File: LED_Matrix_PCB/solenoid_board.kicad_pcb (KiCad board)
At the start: 2 copper layers, 100 x 93 mm, 102 parts, among them J2 MCU_LEFT_LEGS, J3 MCU_RIGHT_LEGS

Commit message: Laid footprint geometry. Need to add a capacitor on the RS-485 Transciever.
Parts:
- moved LED8_0 289.5 mm to (61.4, 156.1)
- moved LED7_2 252.5 mm to (85.4, 145.1)
- moved LED7_1 251.2 mm to (73.4, 145.1)
- moved LED7_0 250.2 mm to (61.4, 145.1)
- moved LED7_4 242.4 mm to (109.4, 145.1)
- moved LED4_1 238.8 mm to (73.4, 112.1)
- moved LED5_0 236.4 mm to (61.4, 123.1)
- moved LED6_2 235.5 mm to (85.4, 134.1)
- moved LED6_3 231.2 mm to (97.4, 134.1)
- moved LED8_5 229.1 mm to (121.4, 156.1)
- moved LED8_4 227.5 mm to (109.4, 156.1)
- moved LED8_3 226.3 mm to (97.4, 156.1)
- moved LED6_1 225.5 mm to (73.4, 134.1)
- moved LED8_2 225.5 mm to (85.4, 156.1)
- moved LED3_0 225.4 mm to (61.4, 101.1)
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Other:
- board outline removed

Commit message: Routed 90% of wires, still need to re-order the column pin masking to better complement the routing.
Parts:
- removed LED8_0, LED8_1, LED8_2, LED8_3, LED8_4, LED8_5, LED8_6, LED8_7, LED8_8: Screw-terminal, TerminalBlock:TerminalBlock_bornier-2_P5.08mm
- moved GND1 8.07 mm to (219.8, 140.3)
- moved LED0_6 4.93 mm to (138.3, 67.9)
- moved LED0_7 4.93 mm to (150.3, 67.9)
- moved LED0_8 4.93 mm to (162.3, 67.9)
- moved LED1_6 4.93 mm to (138.3, 78.9)
- moved LED1_7 4.93 mm to (150.3, 78.9)
- moved LED1_8 4.93 mm to (162.3, 78.9)
- moved LED2_6 4.93 mm to (138.3, 89.9)
- moved LED2_7 4.93 mm to (150.3, 89.9)
- moved LED2_8 4.93 mm to (162.3, 89.9)
- moved LED3_6 4.93 mm to (138.3, 100.9)
- moved LED3_7 4.93 mm to (150.3, 100.9)
- moved LED3_8 4.93 mm to (162.3, 100.9)
- moved LED4_6 4.93 mm to (138.3, 111.9)
- moved LED4_7 4.93 mm to (150.3, 111.9)
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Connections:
- RS-485 pad 2: /A4 -> /MISO
- RS-485 pad 3: /A4 -> /MISO
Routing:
- net /A0: track 0.00 -> 179.2 mm
- net /MOSI: track 0.00 -> 171.2 mm
- net /A1: track 0.00 -> 168.7 mm
- net /ROW6: track 0.00 -> 165.6 mm
- net /A2: track 0.00 -> 163.1 mm
- net /A4: track 0.00 -> 160.5 mm
- net /A5: track 0.00 -> 160.3 mm
- net /A3: track 0.00 -> 159.7 mm
- net /COL8: track 0.00 -> 85.7 mm
- net /COL6: track 0.00 -> 85.7 mm
- net /COL5: track 0.00 -> 85.7 mm
- net /COL4: track 0.00 -> 85.7 mm
- net /COL1: track 0.00 -> 85.7 mm
- net /COL0: track 0.00 -> 85.7 mm
- net /COL7: track 0.00 -> 85.7 mm
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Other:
- board text added: "Author: Patrick Taliaferro"
- board text removed: "Authors: Patrick Taliaferro"
- board text removed: "Will Tekulve"

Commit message: Placed finishing touches on V1.0
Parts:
- added REF**: MountingHole_2.7mm_M2.5, MountingHole:MountingHole_2.7mm_M2.5, F.Cu at (225.0, 145.0)
- added REF**: MountingHole_2.7mm_M2.5, MountingHole:MountingHole_2.7mm_M2.5, F.Cu at (225.0, 35.0)
- added REF**: MountingHole_2.7mm_M2.5, MountingHole:MountingHole_2.7mm_M2.5, F.Cu at (55.0, 35.0)
- added REF**: MountingHole_2.7mm_M2.5, MountingHole:MountingHole_2.7mm_M2.5, F.Cu at (55.0, 145.0)
- moved +5V_IN1 19.4 mm to (218.5, 47.8)
- moved LED6_6 10.8 mm to (133.5, 124.3)
- moved LED6_7 10.8 mm to (145.5, 124.3)
- moved LED6_8 10.8 mm to (157.5, 124.3)
- moved LED7_6 10.8 mm to (133.5, 135.3)
- moved LED7_7 10.8 mm to (145.5, 135.3)
- moved LED7_8 10.8 mm to (157.5, 135.3)
- moved LED6_0 10.8 mm to (61.5, 124.3)
- moved LED7_0 10.8 mm to (61.5, 135.3)
- moved GND1 10.8 mm to (215.0, 130.6)
- moved J2 10.8 mm to (189.2, 77.9)
- moved LED0_6 10.8 mm to (133.5, 58.3)
- moved LED0_7 10.8 mm to (145.5, 58.3)
- moved LED0_8 10.8 mm to (157.5, 58.3)
- moved LED1_6 10.8 mm to (133.5, 69.3)
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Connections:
- R330 pad 2: /SDA -> /D13
- R331 pad 2: /SCL -> /D12
- R332 pad 2: /D5 -> /D11
- R333 pad 2: /D6 -> /D10
- R335 pad 2: /D10 -> /D6
- R336 pad 2: /D11 -> /D5
- R337 pad 2: /D12 -> /SCL
- R338 pad 2: /D13 -> /SDA
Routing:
- net /D12: track 0.00 -> 209.3 mm, vias 0 -> 2
- net /D13: track 0.00 -> 208.6 mm, vias 0 -> 2
- net /D11: track 0.00 -> 208.6 mm, vias 0 -> 2
- net /D10: track 0.00 -> 164.5 mm
- net /D9: track 0.00 -> 150.8 mm
- net /D6: track 0.00 -> 137.5 mm
- net /D5: track 0.00 -> 124.1 mm
- net /SCL: track 0.00 -> 109.9 mm
- net /SDA: track 0.00 -> 96.3 mm
- net +5V: track 0.00 -> 47.5 mm
- net GND: track 0.00 -> 7.13 mm, vias 0 -> 1
- added copper zone on B.Cu, net GND
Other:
- board outline added: 180 x 120 mm

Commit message: Changed footprints for resistors, changed resistor suppliers, and re-routed wires. Need to add mounting holes and clean for ordering.
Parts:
- removed REF** (x4): MountingHole_2.7mm_M2.5, MountingHole:MountingHole_2.7mm_M2.5
- R10, R11, R330, R331, R332, R333, R334, R335, R336, R337, R338: footprint Resistor_SMD:R_2010_5025Metric_Pad1.52x2.65mm_HandSolder -> Resistor_THT:R_Axial_DIN0309_L9.0mm_D3.2mm_P20.32mm_Horizontal
- moved R10 20.5 mm to (179.3, 143.7)
- moved R11 20.4 mm to (173.7, 141.7)
- moved RJ0 13.8 mm to (191.0, 137.0)
- moved RJ1 13.8 mm to (212.2, 137.0)
- moved R330 13.3 mm to (61.5, 34.0), turned to 0 degrees
- moved R331 9.28 mm to (73.5, 38.0), turned to 0 degrees
- moved R335 9.28 mm to (121.5, 38.0), turned to 0 degrees
- moved R332 5.28 mm to (85.5, 42.0), turned to 0 degrees
- moved R336 5.28 mm to (133.5, 42.0), turned to 0 degrees
- moved R334 2.72 mm to (109.5, 50.0), turned to 0 degrees
- moved R338 2.72 mm to (157.5, 50.0), turned to 0 degrees
- moved GND1 2.15 mm to (215.6, 128.5)
- moved R333 1.28 mm to (97.5, 46.0), turned to 0 degrees
- moved R337 1.28 mm to (145.5, 46.0), turned to 0 degrees
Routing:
- net /D11: track 208.6 -> 156.4 mm, vias 2 -> 0
- net /D12: track 209.3 -> 162.2 mm, vias 2 -> 0
- net /D13: track 208.6 -> 172.9 mm, vias 2 -> 0
- net /D10: track 164.5 -> 144.7 mm
- net /D9: track 150.8 -> 131.6 mm
- net /D6: track 137.5 -> 119.4 mm
- net /D5: track 124.1 -> 106.7 mm
- net /SCL: track 109.9 -> 94.2 mm
- net /COL0: track 85.7 -> 101.3 mm
- net /SDA: track 96.3 -> 84.1 mm
- net /RJ45_4: track 41.3 -> 53.0 mm, vias 1 -> 0
- net /COL5: track 85.7 -> 97.3 mm
- net /COL1: track 85.7 -> 97.3 mm
- net Net-(Prt_IC1-Pad2): track 3.45 -> 13.1 mm
- net Net-(Prt_IC1-Pad1): track 9.46 -> 18.7 mm
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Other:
- board size 180 x 120 mm -> 180 x 125 mm

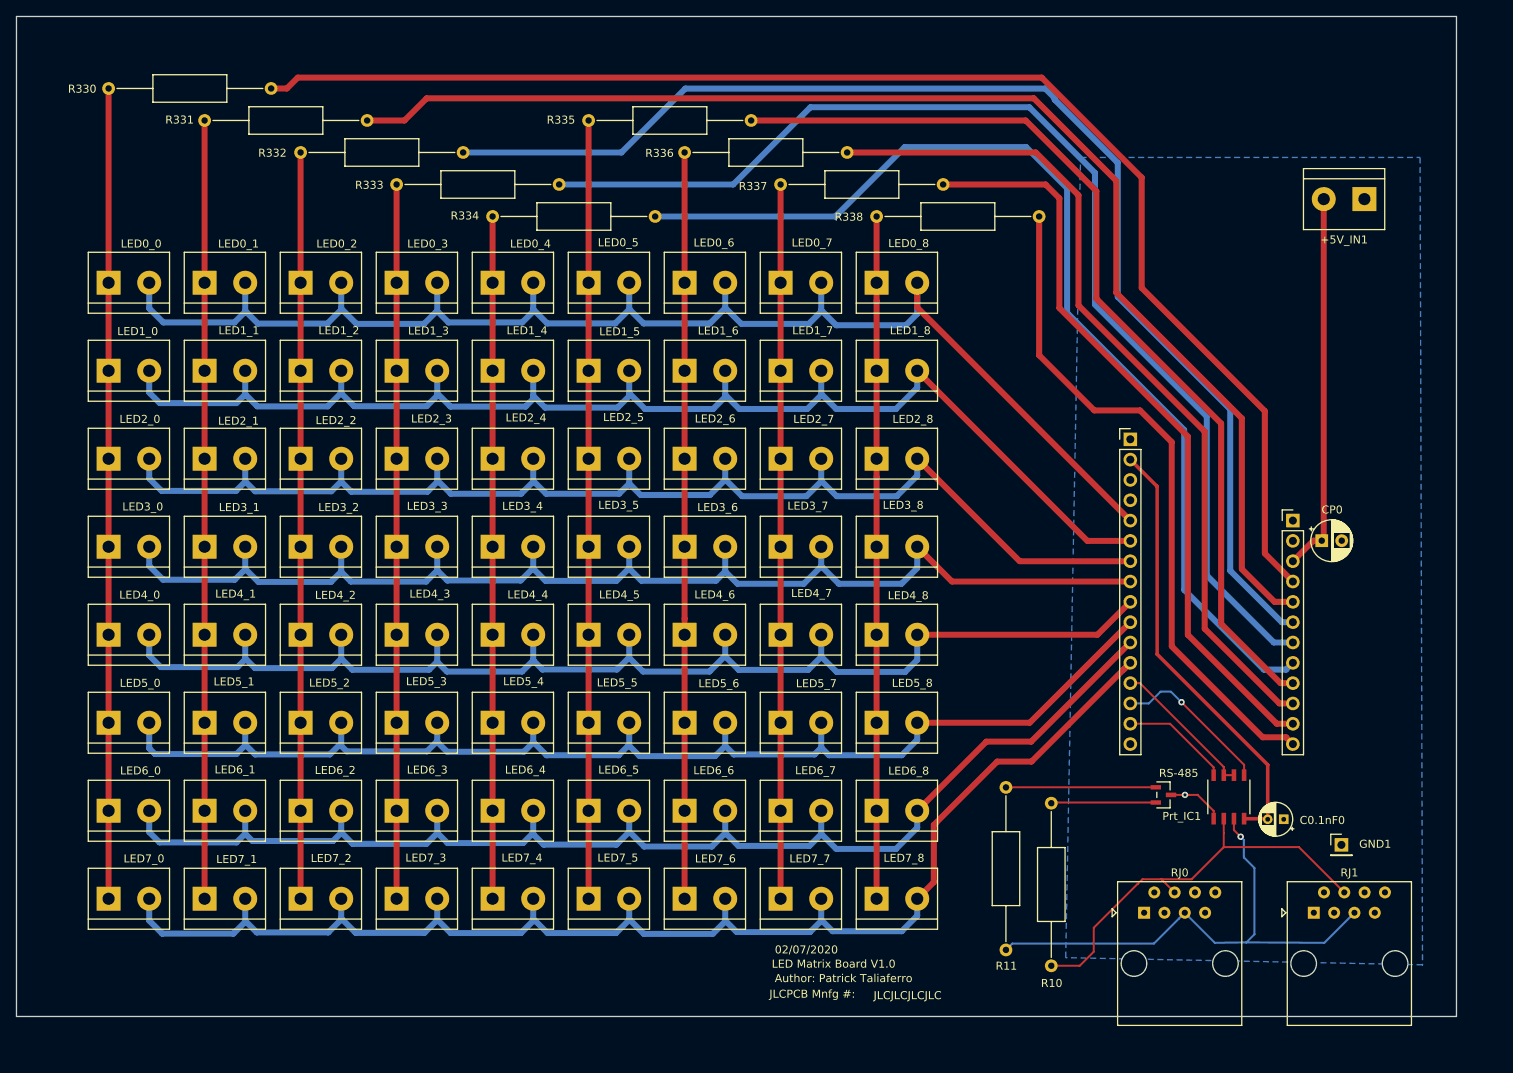
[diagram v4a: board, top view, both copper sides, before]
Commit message: Added Mounting Holes
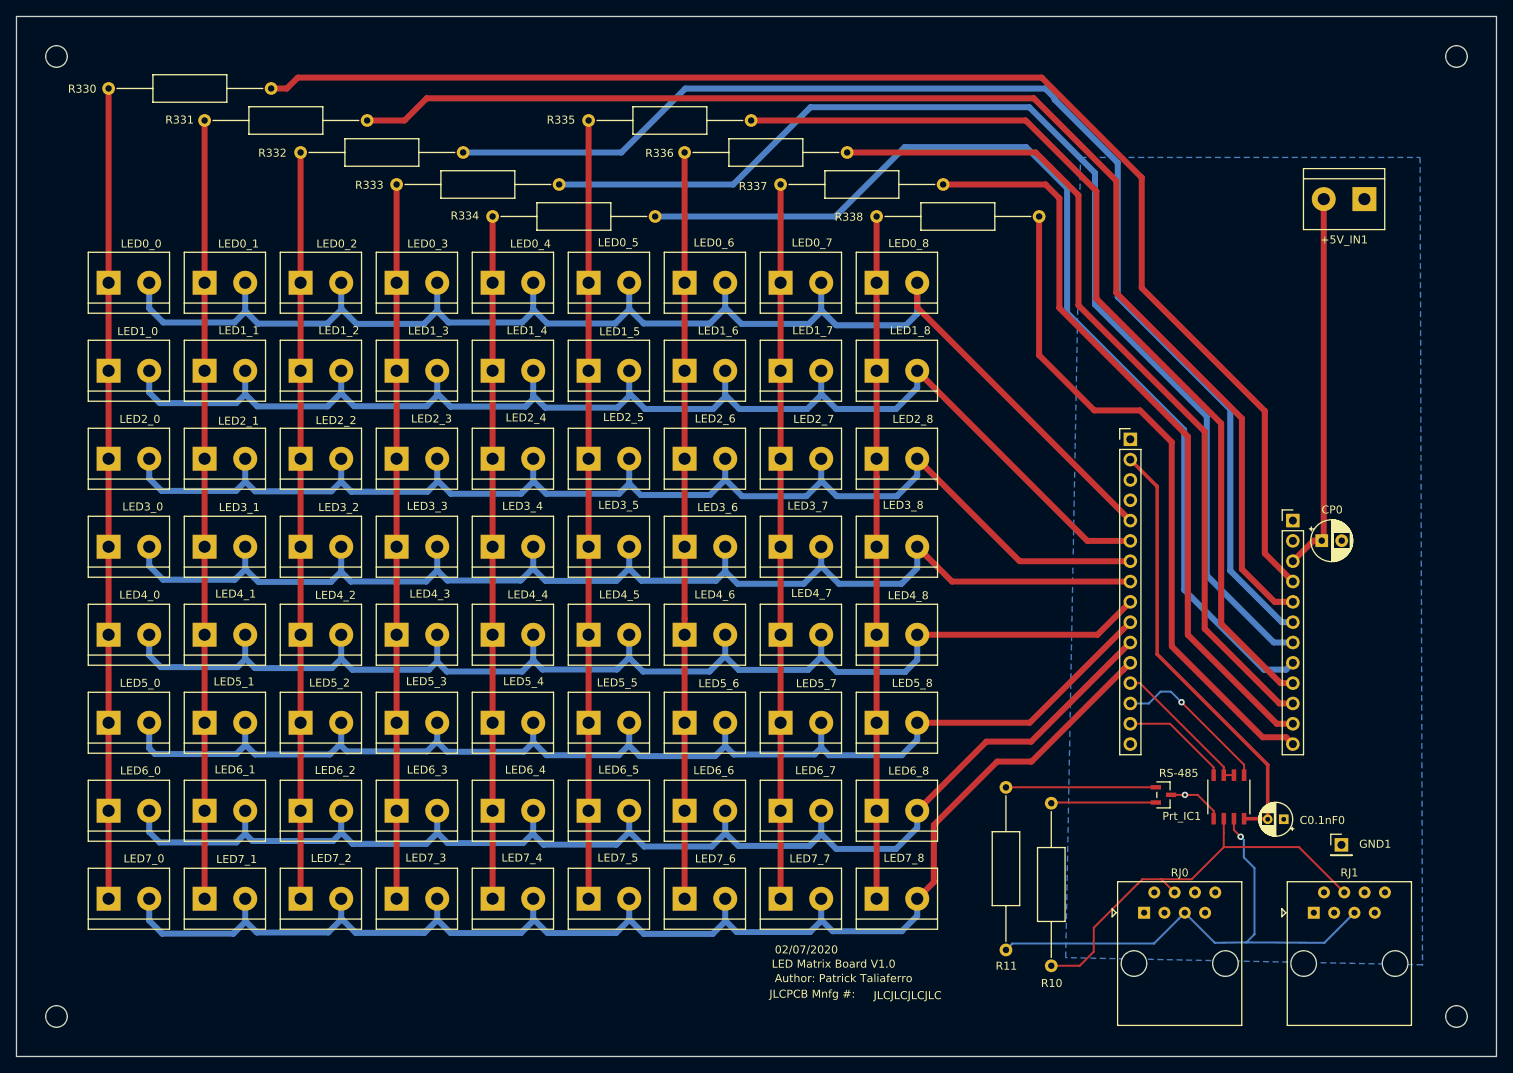
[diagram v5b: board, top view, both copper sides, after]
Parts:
- added REF**: MountingHole_2.7mm_M2.5, MountingHole:MountingHole_2.7mm_M2.5, F.Cu at (230.0, 150.0)
- added REF**: MountingHole_2.7mm_M2.5, MountingHole:MountingHole_2.7mm_M2.5, F.Cu at (55.0, 150.0)
- added REF**: MountingHole_2.7mm_M2.5, MountingHole:MountingHole_2.7mm_M2.5, F.Cu at (55.0, 30.0)
- added REF**: MountingHole_2.7mm_M2.5, MountingHole:MountingHole_2.7mm_M2.5, F.Cu at (230.0, 30.0)
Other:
- board size 180 x 125 mm -> 185 x 130 mm
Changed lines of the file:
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@@
     (tracks 504)
     (zones 0)
-    (modules 93)
+    (modules 97)
     (nets 37)
   )
@@
     (add_net /A4)
     (add_net /A5)
-    (add_net /ARf)
-    (add_net /BAT)
     (add_net /COL0)
     (add_net /COL1)
@@
     (add_net /D6)
     (add_net /D9)
-    (add_net /En)
     (add_net /MISO)
     (add_net /MOSI)
@@
     (add_net /RJ45_5)
     (add_net /ROW6)
-    (add_net /RST)
     (add_net /RX0)
     (add_net /SCL)
@@
     (add_net "Net-(Prt_IC1-Pad1)")
     (add_net "Net-(Prt_IC1-Pad2)")
-    (add_net "Net-(RJ0-Pad1)")
-    (add_net "Net-(RJ0-Pad2)")
-    (add_net "Net-(RJ0-Pad3)")
-    (add_net "Net-(RJ0-Pad6)")
-    (add_net "Net-(RJ0-Pad7)")
-    (add_net "Net-(RJ0-Pad8)")
-    (add_net "Net-(RJ1-Pad1)")
-    (add_net "Net-(RJ1-Pad2)")
-    (add_net "Net-(RJ1-Pad3)")
-    (add_net "Net-(RJ1-Pad6)")
-    (add_net "Net-(RJ1-Pad7)")
-    (add_net "Net-(RJ1-Pad8)")
   )
   (net_class HV ""
@@
     (uvia_drill 0.1)
   )
+  (module MountingHole:MountingHole_2.7mm_M2.5 (layer F.Cu)
+    (at 230 150)
+    (descr "Mounting Hole 2.7mm, no annular, M2.5")
+    (tags "mounting hole 2.7mm no annular m2.5")
+    (attr virtual)
+    (fp_text reference REF** (at 0 -3.7) (layer F.SilkS) hide
+      (effects (font (size 1 1) (thickness 0.15)))
+    )
+    (fp_text value MountingHole_2.7mm_M2.5 (at 0 3.7) (layer F.Fab) hide
+      (effects (font (size 1 1) (thickness 0.15)))
+    )
+    (fp_circle (center 0 0) (end 2.95 0) (layer F.CrtYd) (width 0.05))
+    (fp_circle (center 0 0) (end 2.7 0) (layer Cmts.User) (width 0.15))
+    (fp_text user %R (at 0.3 0) (layer F.Fab) hide
+      (effects (font (size 1 1) (thickness 0.15)))
+    )
+    (pad 1 np_thru_hole circle (at 0 0) (size 2.7 2.7) (drill 2.7) (layers *.Cu *.Mask))
+  )
+  (module MountingHole:MountingHole_2.7mm_M2.5 (layer F.Cu)
+    (at 55 150)
+    (descr "Mounting Hole 2.7mm, no annular, M2.5")
+    (tags "mounting hole 2.7mm no annular m2.5")
+    (attr virtual)
+    (fp_text reference REF** (at 0 -3.7) (layer F.SilkS) hide
+      (effects (font (size 1 1) (thickness 0.15)))
+    )
+    (fp_text value MountingHole_2.7mm_M2.5 (at 0 3.7) (layer F.Fab) hide
+      (effects (font (size 1 1) (thickness 0.15)))
+    )
+    (fp_circle (center 0 0) (end 2.95 0) (layer F.CrtYd) (width 0.05))
+    (fp_circle (center 0 0) (end 2.7 0) (layer Cmts.User) (width 0.15))
+    (fp_text user %R (at 0.3 0) (layer F.Fab) hide
+      (effects (font (size 1 1) (thickness 0.15)))
+    )
+    (pad 1 np_thru_hole circle (at 0 0) (size 2.7 2.7) (drill 2.7) (layers *.Cu *.Mask))
+  )
+  (module MountingHole:MountingHole_2.7mm_M2.5 (layer F.Cu)
+    (at 55 30)
+    (descr "Mounting Hole 2.7mm, no annular, M2.5")
+    (tags "mounting hole 2.7mm no annular m2.5")
+    (attr virtual)
+    (fp_text reference REF** (at 0 -3.7) (layer F.SilkS) hide
+      (effects (font (size 1 1) (thickness 0.15)))
+    )
+    (fp_text value MountingHole_2.7mm_M2.5 (at 0 3.7) (layer F.Fab) hide
+      (effects (font (size 1 1) (thickness 0.15)))
+    )
+    (fp_circle (center 0 0) (end 2.95 0) (layer F.CrtYd) (width 0.05))
+    (fp_circle (center 0 0) (end 2.7 0) (layer Cmts.User) (width 0.15))
+    (fp_text user %R (at 0.3 0) (layer F.Fab) hide
+      (effects (font (size 1 1) (thickness 0.15)))
+    )
+    (pad 1 np_thru_hole circle (at 0 0) (size 2.7 2.7) (drill 2.7) (layers *.Cu *.Mask))
+  )
+  (module MountingHole:MountingHole_2.7mm_M2.5 (layer F.Cu)
+    (at 230 30)
+    (descr "Mounting Hole 2.7mm, no annular, M2.5")
+    (tags "mounting hole 2.7mm no annular m2.5")
+    (attr virtual)
+    (fp_text reference REF** (at 0 -3.7) (layer F.SilkS) hide
+      (effects (font (size 1 1) (thickness 0.15)))
+    )
+    (fp_text value MountingHole_2.7mm_M2.5 (at 0 3.7) (layer F.Fab) hide
+      (effects (font (size 1 1) (thickness 0.15)))
+    )
+    (fp_circle (center 0 0) (end 2.95 0) (layer F.CrtYd) (width 0.05))
+    (fp_circle (center 0 0) (end 2.7 0) (layer Cmts.User) (width 0.15))
+    (fp_text user %R (at 0.3 0) (layer F.Fab) hide
+      (effects (font (size 1 1) (thickness 0.15)))
+    )
+    (pad 1 np_thru_hole circle (at 0 0) (size 2.7 2.7) (drill 2.7) (layers *.Cu *.Mask))
+  )
   (module Resistor_THT:R_Axial_DIN0309_L9.0mm_D3.2mm_P20.32mm_Horizontal (layer F.Cu)
     (at 173.6852 141.6812 90)
@@
     )
   )
-  (gr_line (start 50 25) (end 50 150) (layer Edge.Cuts) (width 0.12))
-  (gr_line (start 230 25) (end 50 25) (layer Edge.Cuts) (width 0.12))
-  (gr_line (start 230 150) (end 230 25) (layer Edge.Cuts) (width 0.12))
-  (gr_line (start 50 150) (end 230 150) (layer Edge.Cuts) (width 0.12))
+  (gr_line (start 50 25) (end 50 155) (layer Edge.Cuts) (width 0.12))
+  (gr_line (start 235 25) (end 50 25) (layer Edge.Cuts) (width 0.12))
+  (gr_line (start 235 155) (end 235 25) (layer Edge.Cuts) (width 0.12))
+  (gr_line (start 50 155) (end 235 155) (layer Edge.Cuts) (width 0.12))
   (gr_text JLCJLCJLCJLC (at 161.3916 147.3708) (layer F.SilkS)
     (effects (font (size 1 1) (thickness 0.15)))
